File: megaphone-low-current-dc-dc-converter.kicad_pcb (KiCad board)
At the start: 2 copper layers, 13.8 x 21.9 mm, 9 parts, among them U1 U1=TPS631000DRLR

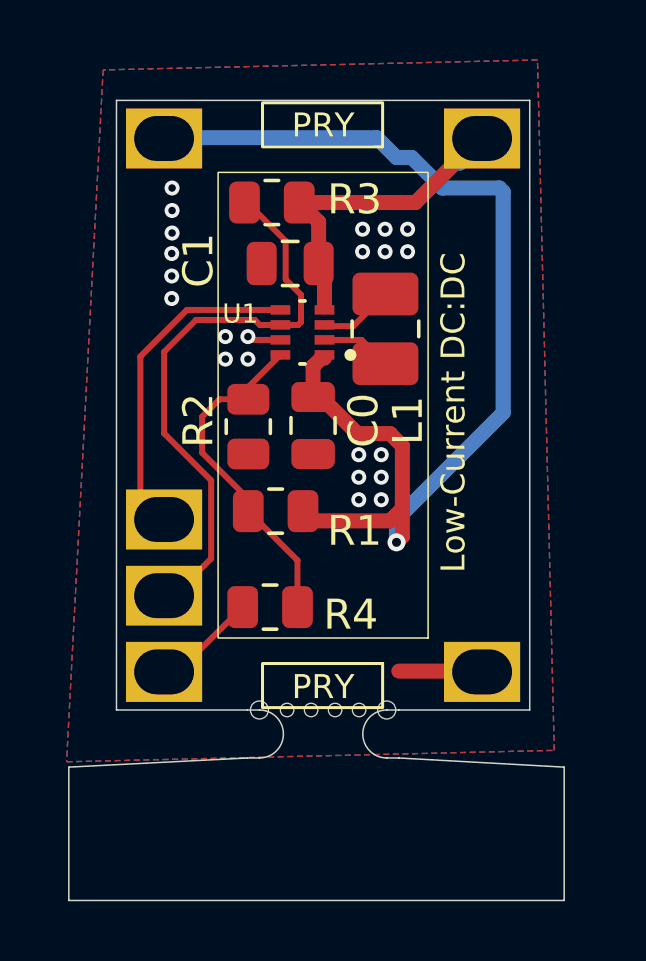
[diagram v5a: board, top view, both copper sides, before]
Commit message: Updating footprint, and re-routing
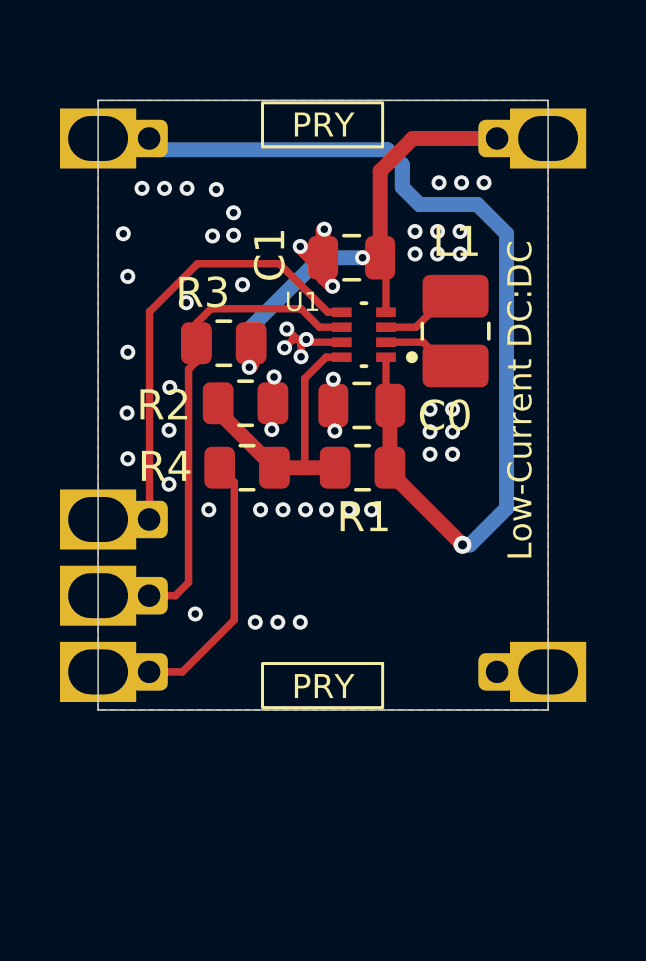
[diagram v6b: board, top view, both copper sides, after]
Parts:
- M2: footprint MegaCastle:MegaCastle2x8-Module-I7.0x15.5-M8187-PANEL-NIBBLE -> megaphone-low-current-dc-dc-converter Footprint Library:MegaCastle2x8-Module-I15.0x15.5-M8187-SPAREPAD
- U1: value U1=TPS631000DRLR -> TPS631000DRLR
- moved R3 4.96 mm to (116.9, 73.5)
- moved R4 4.71 mm to (117.7, 77.7)
- moved R1 3.24 mm to (121.5, 77.7)
- moved L1 2.34 mm to (124.7, 73.1)
- moved C1 2.06 mm to (121.2, 70.7)
- moved U1 2.05 mm to (121.6, 73.2)
- moved C0 1.76 mm to (121.5, 75.6), turned to 180 degrees
- moved R2 0.78 mm to (117.7, 75.5), turned to 0 degrees
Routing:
- net VOUT: track 38.6 -> 32.3 mm
- net MODE: track 21.8 -> 15.5 mm
- net GND: track 3.85 -> 9.99 mm, vias 22 -> 54
- net VBAT: track 11.9 -> 16.6 mm, vias 0 -> 2
- net SEL1V8: track 4.44 -> 8.83 mm
- net EN: track 11.1 -> 14.7 mm
- net Net-(U1-FB): track 11.4 -> 9.46 mm
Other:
- board size 13.8 x 21.9 mm -> 15 x 20.3 mm
